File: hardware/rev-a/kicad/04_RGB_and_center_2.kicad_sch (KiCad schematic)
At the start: 11 parts

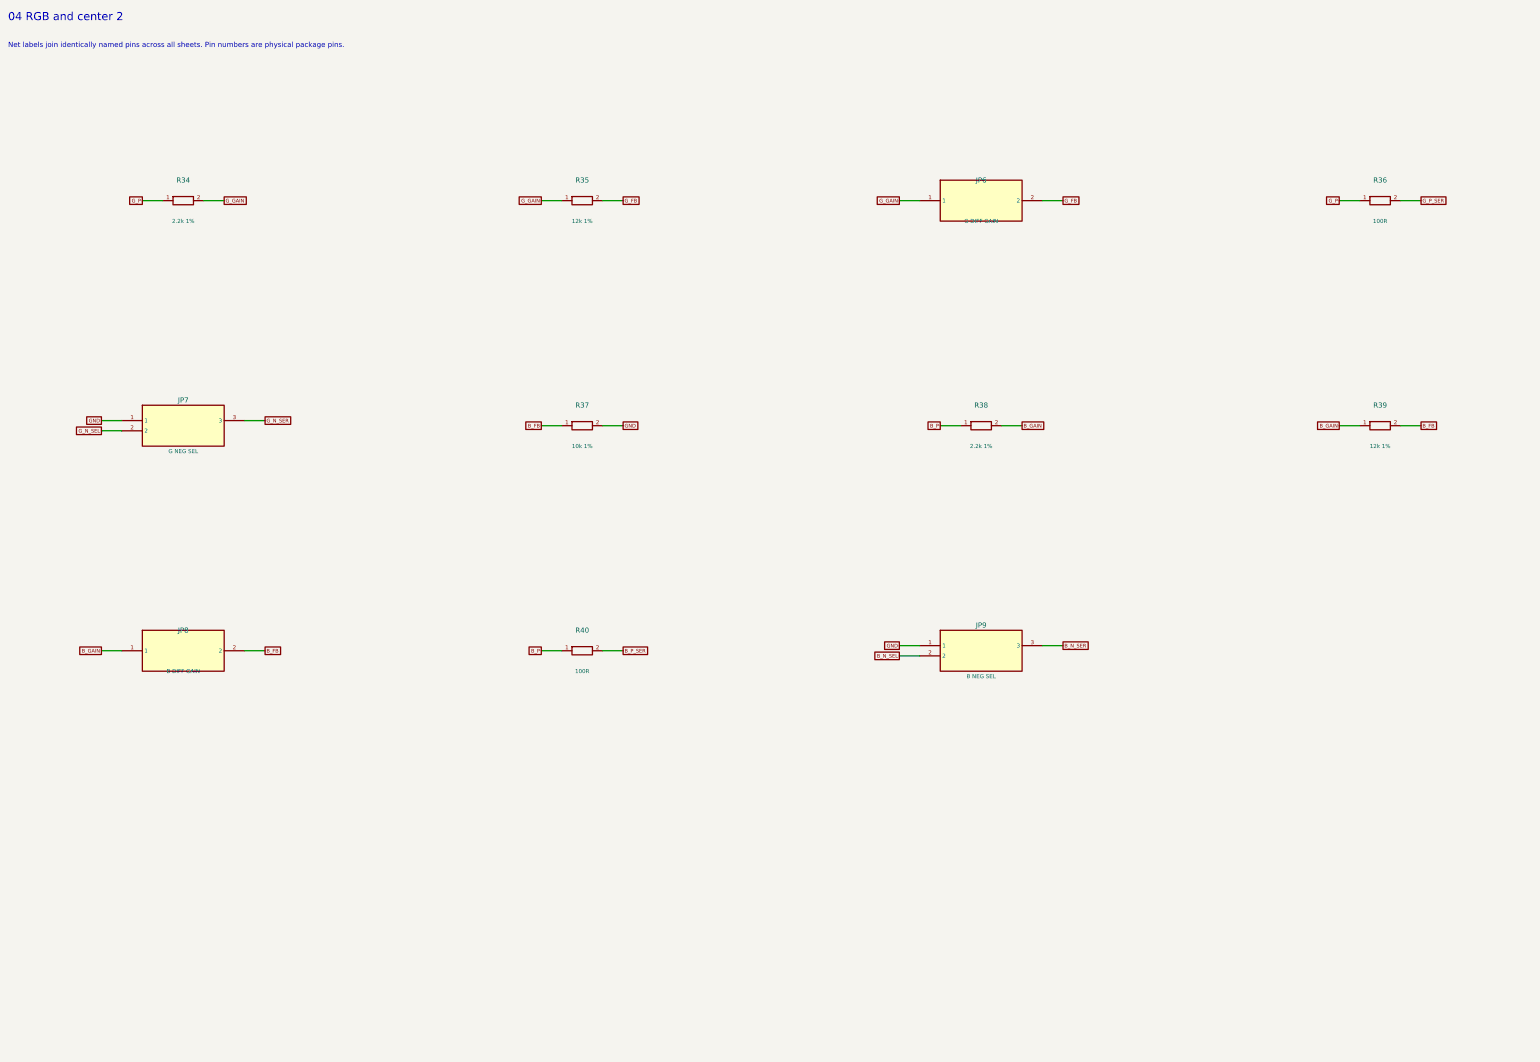
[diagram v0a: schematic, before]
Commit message: Redraw Rev.A schematics with functional blocks and explicit wiring
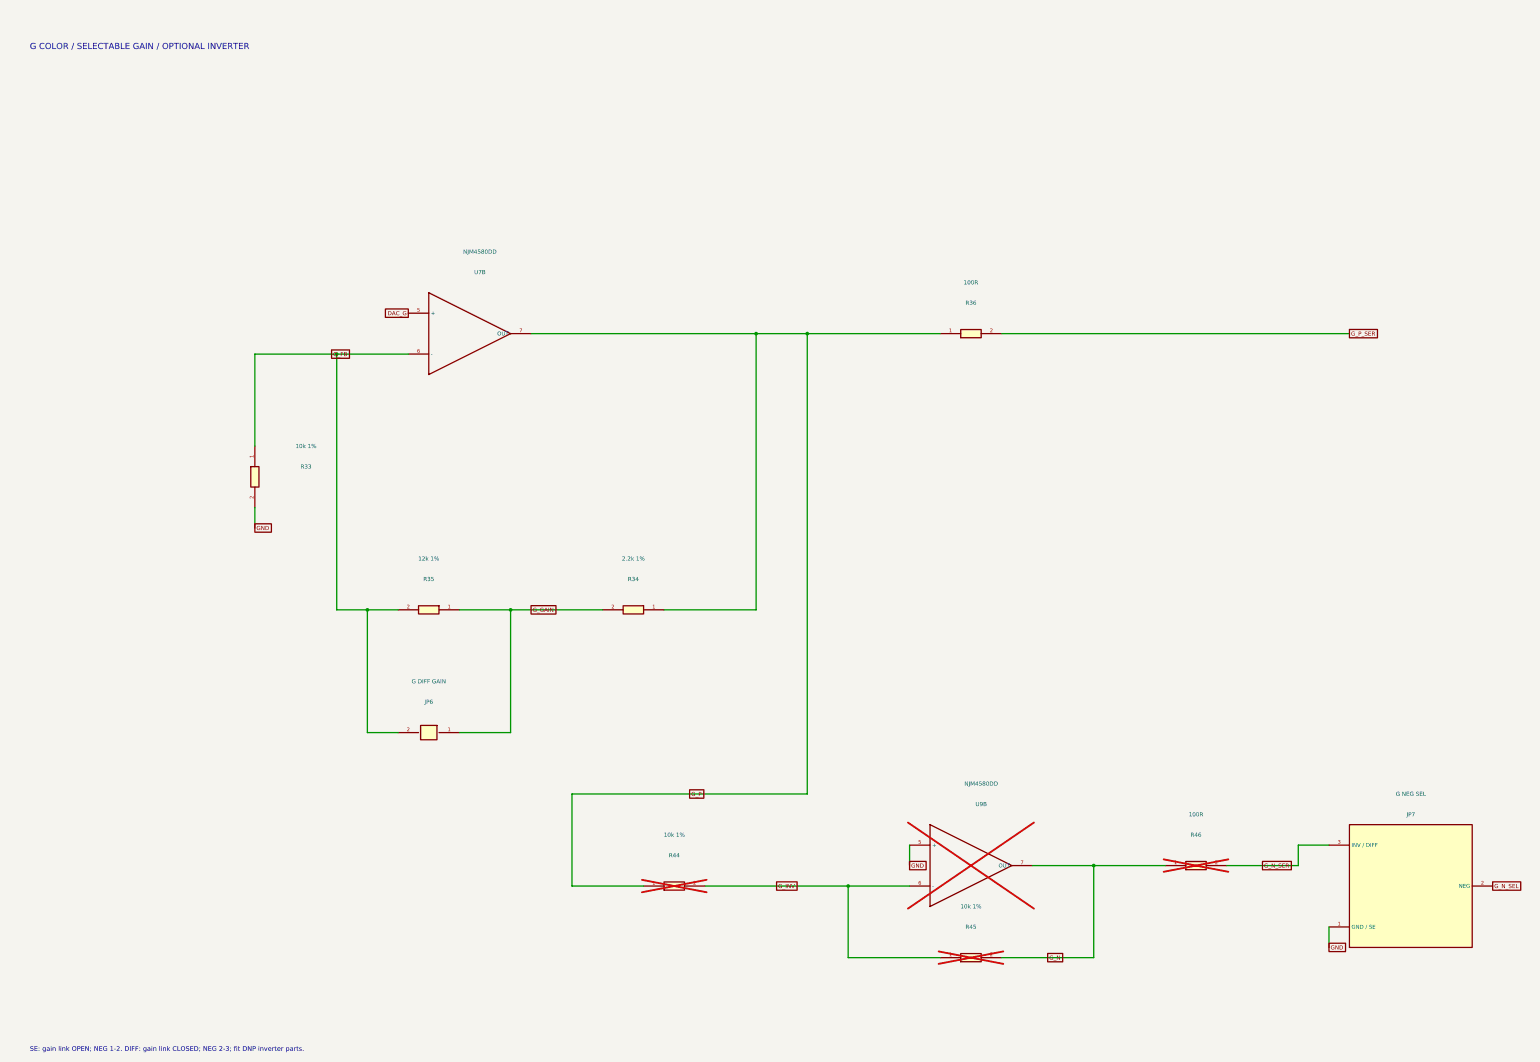
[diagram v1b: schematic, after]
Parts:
- removed JP8: B DIFF GAIN, RevA:PinHeader_1x02_P2.54mm_Vertical, symbol RevA:Conn_JP8
- removed JP9: B NEG SEL, RevA:PinHeader_1x03_P2.54mm_Vertical, symbol RevA:Conn_JP9
- removed R37: 10k 1%, RevA:R_Axial_DIN0207_L6.3mm_D2.5mm_P10.16mm_Horizontal, symbol RevA:R
- removed R38: 2.2k 1%, RevA:R_Axial_DIN0207_L6.3mm_D2.5mm_P10.16mm_Horizontal, symbol RevA:R
- removed R39: 12k 1%, RevA:R_Axial_DIN0207_L6.3mm_D2.5mm_P10.16mm_Horizontal, symbol RevA:R
- removed R40: 100R, RevA:R_Axial_DIN0207_L6.3mm_D2.5mm_P10.16mm_Horizontal, symbol RevA:R
- added R33, R44, R45: 10k 1%, RevA:R_Axial_DIN0207_L6.3mm_D2.5mm_P10.16mm_Horizontal, symbol RevA:R
- added R46: 100R, RevA:R_Axial_DIN0207_L6.3mm_D2.5mm_P10.16mm_Horizontal, symbol RevA:R
- added U7, U9: NJM4580DD, RevA:DIP-8_W7.62mm, symbol RevA:AMP
- JP6: symbol RevA:Conn_JP6 -> RevA:Link
- JP7: symbol RevA:Conn_JP7 -> RevA:Part_JP7
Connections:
- net GND: now also R33.2, U9.5 (+)
- net G_FB: now also R33.1, U7.6 (-)
- net G_N_SER: now also R46.2
- net G_P: now also R44.1, U7.7 (OUT)
- new net DAC_G: U7.5 (+)
- new net G_INV: R44.2, R45.1, U9.6 (-)
- new net G_N: R45.2, R46.1, U9.7 (OUT)
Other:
- note added: "G COLOR / SELECTABLE GAIN / OPTIONAL INVERTER"
- note added: "SE: gain link OPEN; NEG 1-2. DIFF: gain link CLOSED; NEG 2-3; fit DNP inverter parts."
- note removed: "04 RGB and center 2"
- note removed: "Net labels join identically named pins across all sheets. Pin numbers are physical package pins."
- company: CoreS3 ILDA evaluation -> (none)
- title: 04_RGB_and_center_2 -> G / Color driver and optional differential stage
- moved on the sheet: JP7
